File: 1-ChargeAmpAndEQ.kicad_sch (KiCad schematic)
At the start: 55 parts, among them J101 6.3mm stereo, J102 6.3mm stereo, U101 OPA145, U102 OPA145

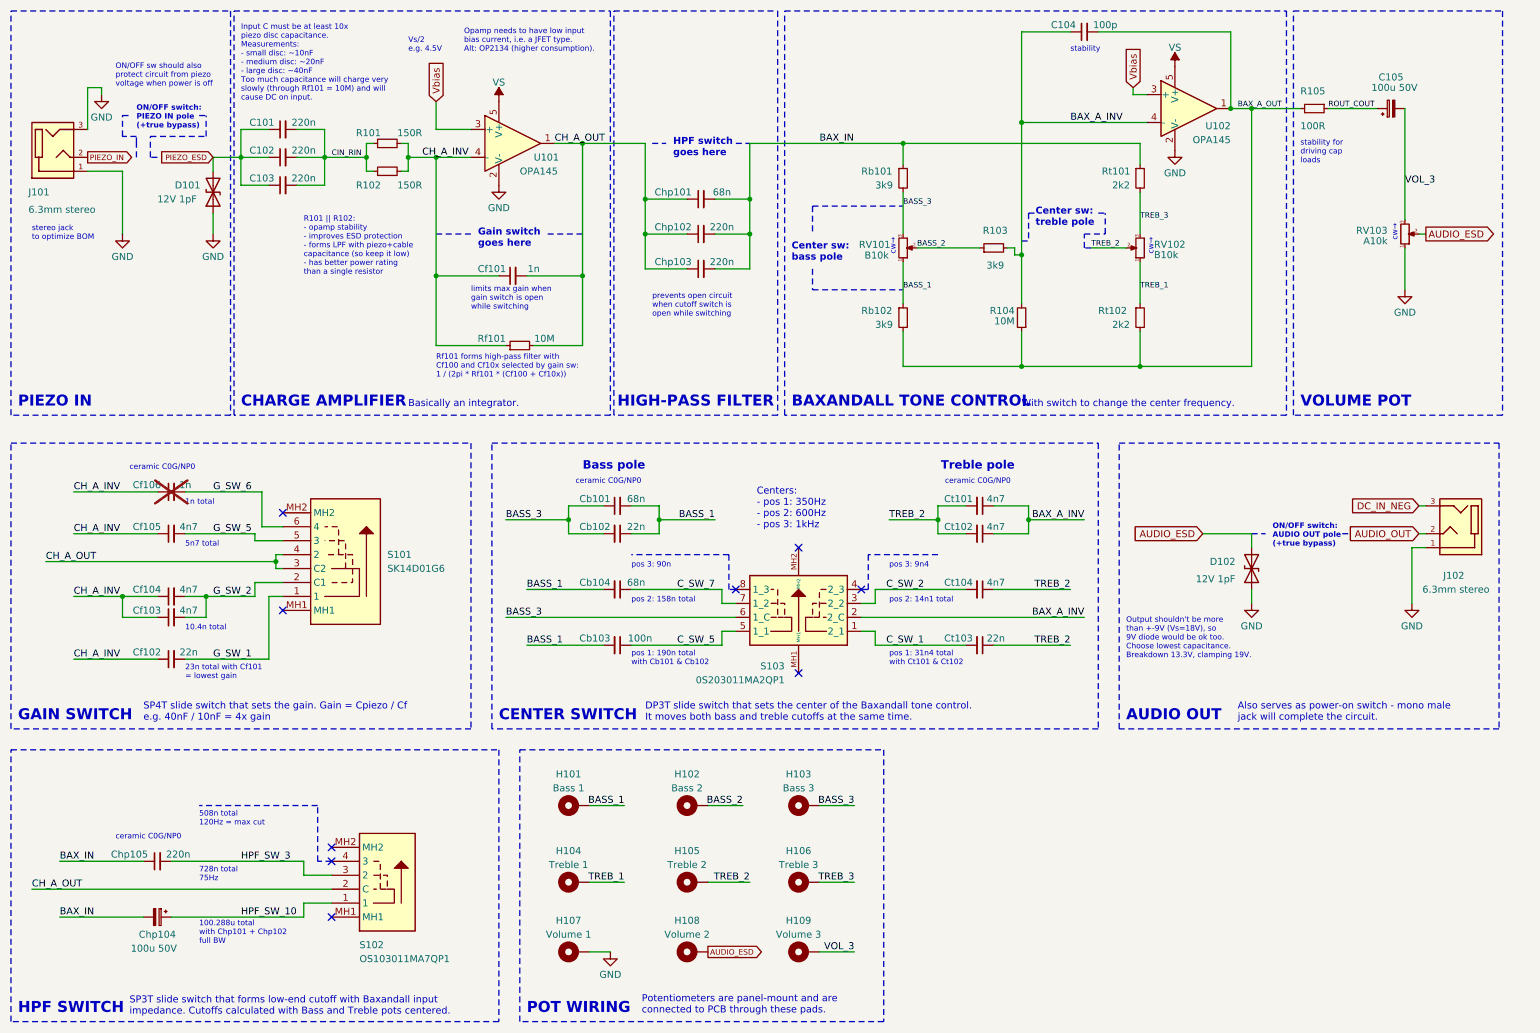
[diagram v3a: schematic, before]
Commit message: Schematic: replacing SP3T HPF switch with SP4T again, adding the new HPF cutoff position, moving libraries around. Choosing different 150R resistor because of availability
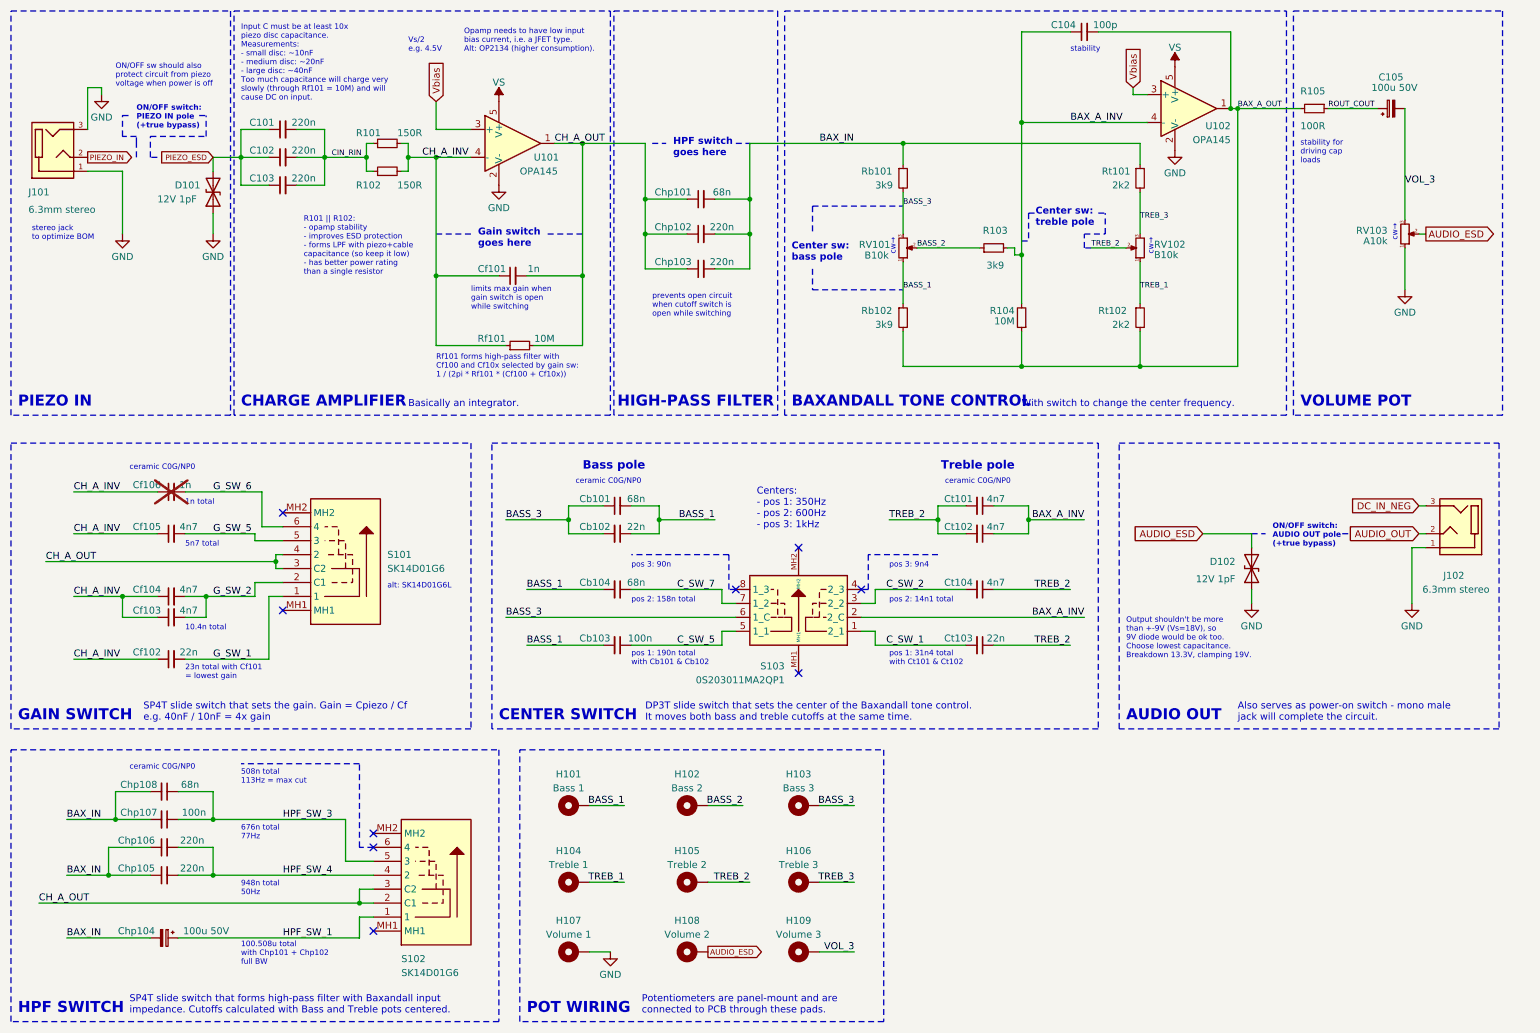
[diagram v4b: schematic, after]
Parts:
- removed S102: OS103011MA7QP1, library:sw_OS103011MA7QP1, symbol sw_OS103011MA7QP1:OS103011MA7QP1
- added Chp105: 220n, library:GRM31C5C1H224JE02L, symbol Device:C_Small
- added Chp107: 100n, library:GRM31C5C2A104JA01L, symbol Device:C_Small
- added Chp108: 68n, library:GRM31C5C1H683JA01L, symbol Device:C_Small
- added S102: SK14D01G6, library:sw_SK14D01G6, symbol sw_SK14D01G6:SK14D01G6
- R101, R102: footprint library:RT0603BRD07150RL_UL-M -> library:RT0603BRE07150RL_UL-M; LCSC Part # C705726 -> C728601; Mfr Part # RT0603BRD07150RL -> RT0603BRE07150RL; Mouser Part # 603-RT0603BRD07150RL -> 603-RT0603BRE07150RL
- renumbered Chp105 to Chp106
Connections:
- net BAX_IN: now also Chp105.1, Chp107.2, Chp108.2
- net CH_A_OUT: now also S102.2 (C1), S102.3 (C2)
- net HPF_SW_3: now also Chp107.1, Chp108.1, S102.5 (3); no longer Chp106.2
- net HPF_SW_10 renamed HPF_SW_1
- net HPF_SW_1: now also S102.1
- new net HPF_SW_4: Chp105.2, Chp106.2, S102.4 (2)
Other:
- note added: "100.508u total with Chp101 + Chp102 full BW"
- note added: "508n total 113Hz = max cut"
- note added: "676n total 77Hz"
- note added: "948n total 50Hz"
- note added: "SP4T slide switch that forms high-pass filter with Baxandall input impedance. Cutoffs calculated with Bass and Treble pots centered."
- note added: "alt: SK14D01G6L"
- note removed: "100.288u total with Chp101 + Chp102 full BW"
- note removed: "508n total 120Hz = max cut"
- note removed: "728n total 75Hz"
- note removed: "SP3T slide switch that forms low-end cutoff with Baxandall input impedance. Cutoffs calculated with Bass and Treble pots centered."
- moved on the sheet: Chp104, Chp106

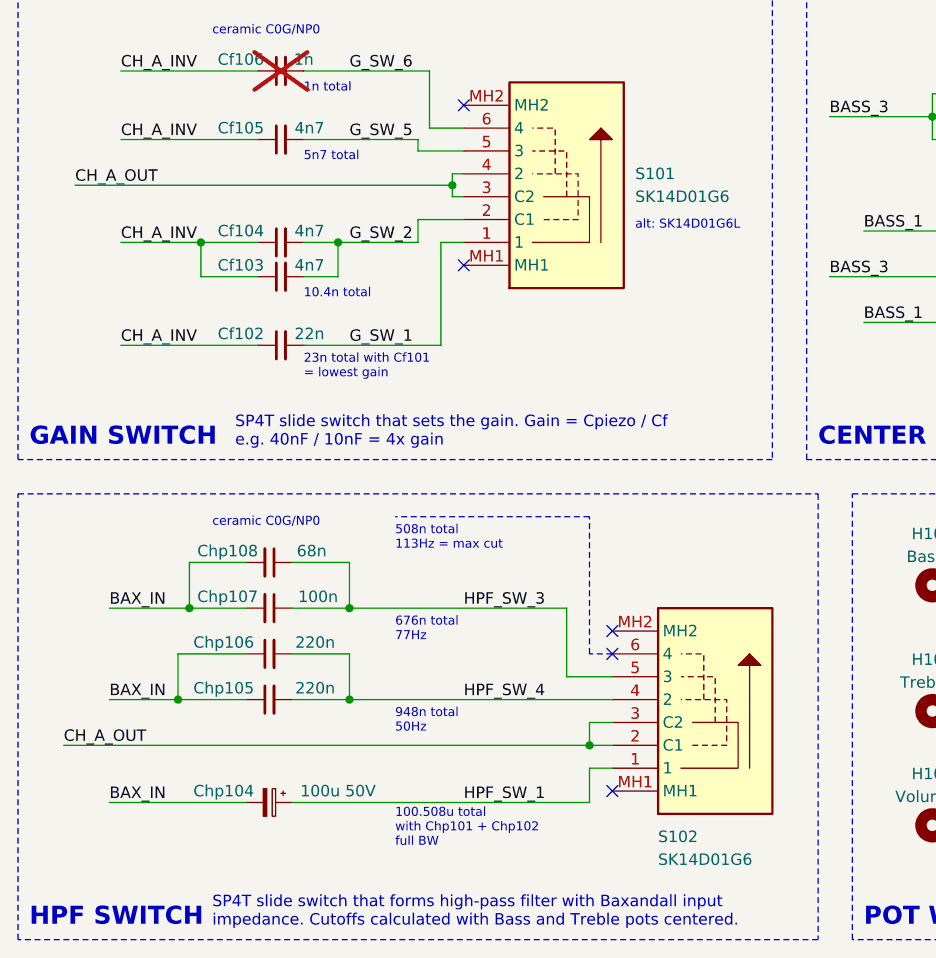
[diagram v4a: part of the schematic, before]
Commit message: schematic: finishing standoffs, screws, minor improvements
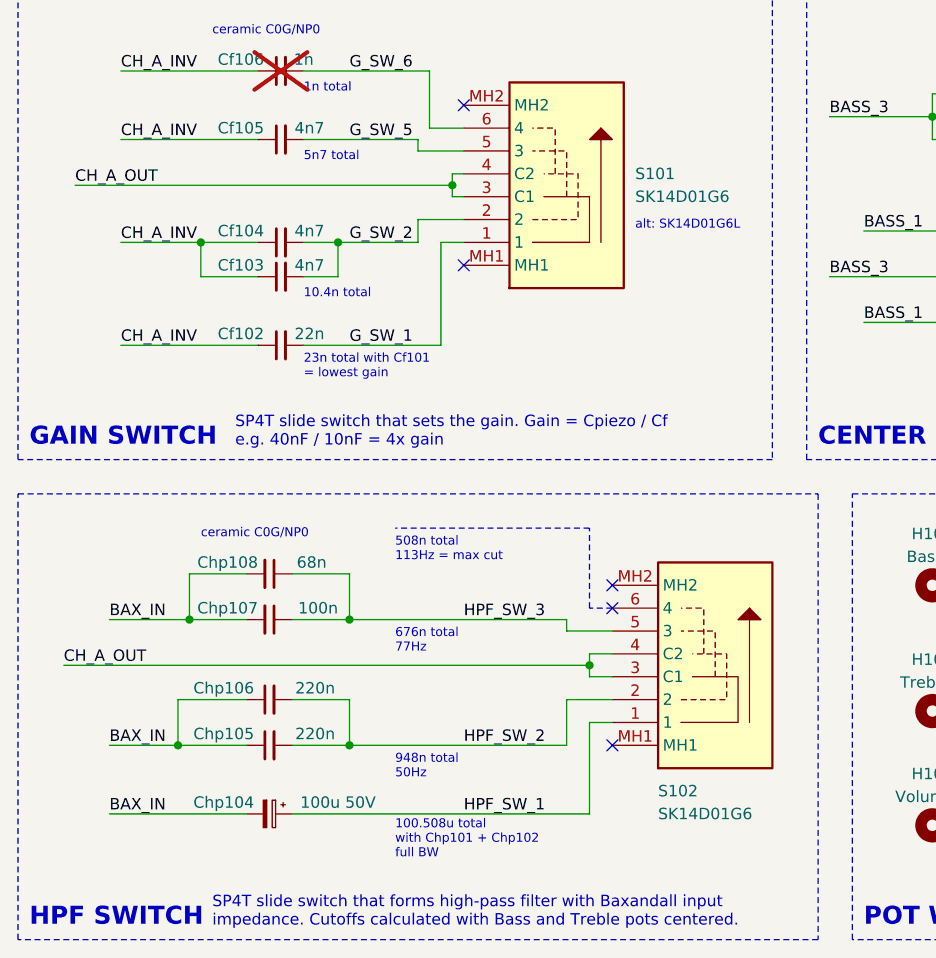
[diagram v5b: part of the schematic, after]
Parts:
- H101, H102, H103, H104, H105, H106, H107, H108, H109: now left out of the parts list
- R104, Rf101, U101, U102: Source Mouser -> LCSC
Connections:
- net CH_A_OUT: now also S102.4 (C2); no longer S102.2 (C1)
- net HPF_SW_4 renamed HPF_SW_2
- net HPF_SW_2: now also S102.2; no longer S102.4 (2)
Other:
- moved on the sheet: Chp104, Chp105, Chp106, Chp107, Chp108, S102

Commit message: Schematics: improving Purpose of some components
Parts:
- S101: Purpose Sets gain (ratio of feedback capacitance vs piezo capacitan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 -> SP4T. Sets gain (ratio of feedback capacitance vs piezo cap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
- S102: Purpose Sets high-pass filter cutoff frequency -> SP4T. Sets high-pass filter cutoff frequency
- S103: Purpose sets Baxandall center frequency -> DP3T. Sets Baxandall center frequency
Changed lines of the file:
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@@
 			)
 		)
-		(property "Purpose" "Sets high-pass filter cutoff frequency"
+		(property "Purpose" "SP4T. Sets high-pass filter cutoff frequency"
 			(at 78.74 175.26 0)
 			(effects
@@
 			)
 		)
-		(property "Purpose" "Sets gain (ratio of feedback capacitance vs piezo capacitance)"
+		(property "Purpose" "SP4T. Sets gain (ratio of feedback capacitance vs piezo capacitance)"
 			(at 62.23 121.92 0)
 			(effects
@@
 			)
 		)
-		(property "Purpose" "sets Baxandall center frequency"
+		(property "Purpose" "DP3T. Sets Baxandall center frequency"
 			(at 156.21 125.73 0)
 			(effects

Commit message: Using larger footprint for DNP feedback cap; small improvements
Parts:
- Cf106: footprint library:GRM1885C1H102JA01D -> library:cap_SMD_DNP
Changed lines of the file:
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@@
 			)
 		)
-		(property "Footprint" "library:GRM1885C1H102JA01D"
+		(property "Footprint" "library:cap_SMD_DNP"
 			(at 41.91 100.33 0)
 			(effects
